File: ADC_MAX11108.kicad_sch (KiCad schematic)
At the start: 60 parts, among them IC22 524SDCGI8, IC24 524SDCGI8, IC26 524SDCGI8, IC28 524SDCGI8, IC30 LMS1585ACSX-ADJ_NOPB, J1 Conn_01x02_Pin, J2 Conn_01x03_Pin, J3 Conn_01x07_Pin, J4 Conn_01x07_Pin, J5 Conn_01x07_Pin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

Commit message: completed duplicating the ADCs in the schematic
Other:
- added sheet ADC10 (untitled.kicad_sch)
- added sheet ADC11 (untitled.kicad_sch)
- added sheet ADC12 (untitled.kicad_sch)
- added sheet ADC13 (untitled.kicad_sch)
- added sheet ADC14 (untitled.kicad_sch)
- added sheet ADC15 (untitled.kicad_sch)
- added sheet ADC16 (untitled.kicad_sch)
- added sheet ADC17 (untitled.kicad_sch)
- added sheet ADC18 (untitled.kicad_sch)
- added sheet ADC19 (untitled.kicad_sch)
- added sheet ADC2 (untitled.kicad_sch)
- added sheet ADC20 (untitled.kicad_sch)
- added sheet ADC21 (untitled.kicad_sch)
- added sheet ADC22 (untitled.kicad_sch)
- added sheet ADC23 (untitled.kicad_sch)
- added sheet ADC24 (untitled.kicad_sch)
- added sheet ADC3 (untitled.kicad_sch)
- added sheet ADC4 (untitled.kicad_sch)
- added sheet ADC5 (untitled.kicad_sch)
- added sheet ADC6 (untitled.kicad_sch)
- added sheet ADC7 (untitled.kicad_sch)
- added sheet ADC8 (untitled.kicad_sch)
- added sheet ADC9 (untitled.kicad_sch)

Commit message: Updated schematic and PCB layout, no more precision Vrefs
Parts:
- removed C194, C52, C54, C58, C59: 10uF, Capacitor_SMD:C_0402_1005Metric_Pad0.74x0.62mm_HandSolder, symbol Device:C
- removed C53, C55, C56, C57, C60, C61, C69, C71, C73: 0.1uF, Capacitor_SMD:C_0402_1005Metric_Pad0.74x0.62mm_HandSolder, symbol Device:C
- removed J2: Conn_01x03_Pin, Connector_PinHeader_2.54mm:PinHeader_1x03_P2.54mm_Vertical, symbol Connector:Conn_01x03_Pin
- removed U1, U2, U3, U4, U5: ADR4533, Package_SO:SOIC-8_3.9x4.9mm_P1.27mm, symbol Reference_Voltage:ADR4533
- added J2, J8: Conn_01x02_Pin, Connector_PinHeader_2.54mm:PinHeader_1x02_P2.54mm_Vertical, symbol Connector:Conn_01x02_Pin
- C195, C68, C70, C72: value 10uF -> 0.01uF
- C196, C197, C66, C67: value C -> 10uF
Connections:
- net 3.4V is gone; now on net 3.3_ADJ: J1.1 (Pin_1)
- net Battery_3.3V is gone; now on net Vref_LDO: Q1.2 (OUTPUT)
- net Basys_3.3V: now also J2.1 (Pin_1), J2.2 (Pin_2)
- net GND: now also C196.2, C197.2, C66.2, C67.1
- net Switch_out: now also C197.1, C67.2
- net at IC30.2 (OUTPUT), IC30.4 (VOUT_1), IC30.5 (VOUT_2)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: now also C196.1
- net Vref_LDO: now reaches C66.1
- net Vref_LDO: now also J8.2 (Pin_2)
- net +3.3V renamed 3.3_ADJ
- new net 3.3VRef: J8.1 (Pin_1)
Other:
- note added: "A 33 OHM series terminating resistor may be used on each clock output if the trace is longer than 1 inch."
- note removed: "A minimum number of external components are required for proper operation. A decoupling capacitor of 0.01µF should be connected between VDD on pin 5 and GND on pin 8, as close to the device as possible. A 33 series terminating resistor may be used on each clock output if the trace is longer than 1 inch."
- moved on the sheet: Barrel_Jack1, C196, C197, C66, C67, IC30, J1, R21, S1, VR1

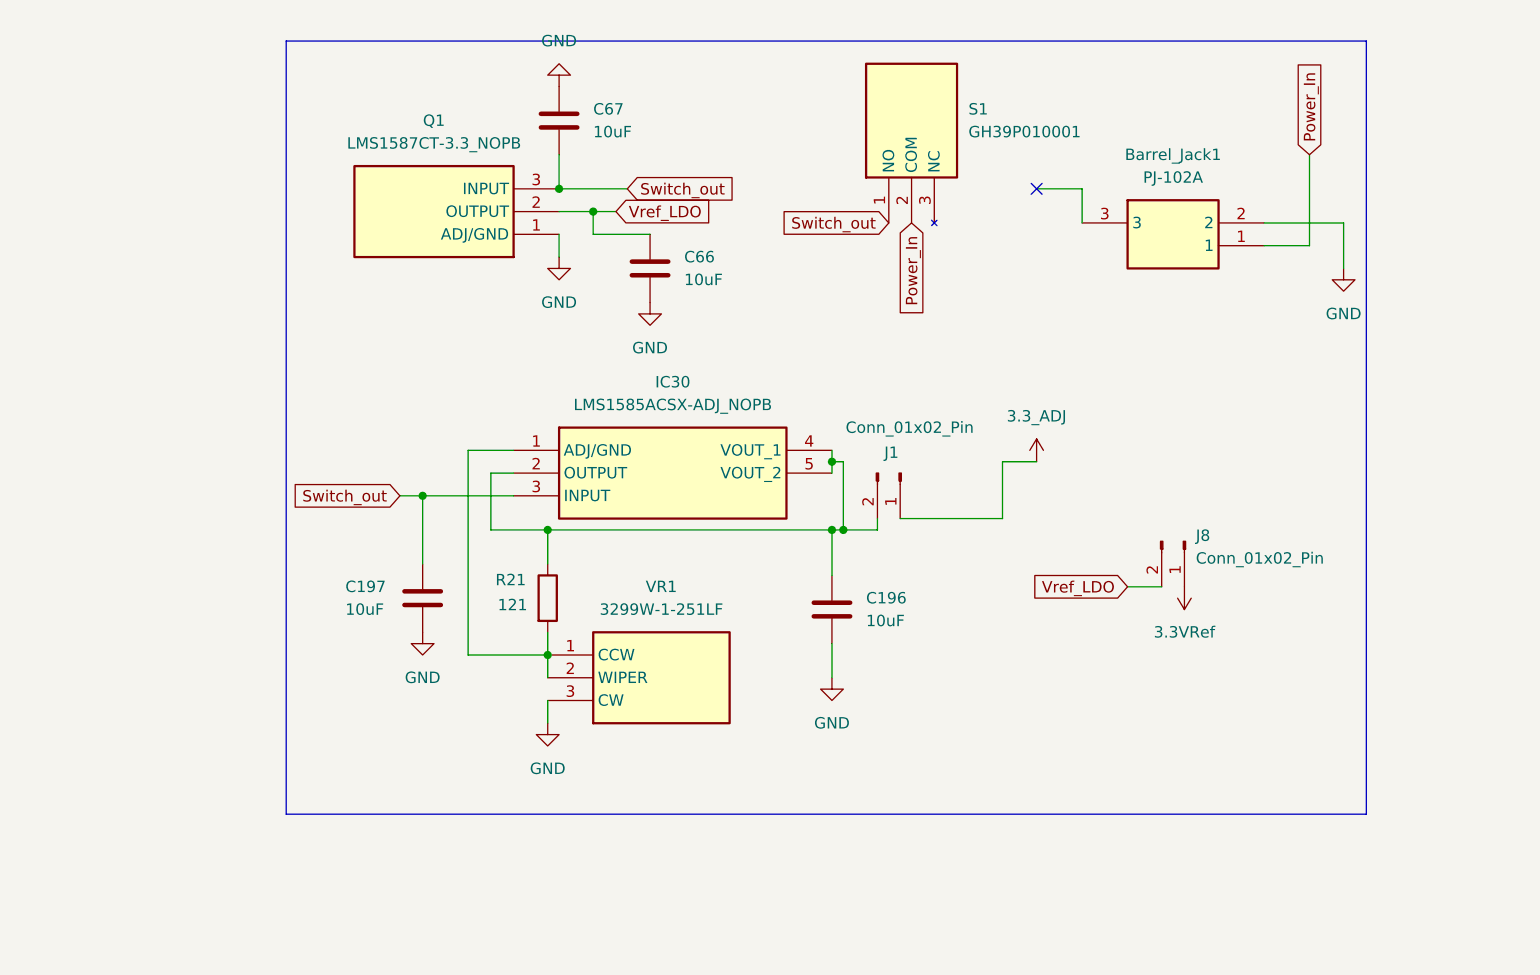
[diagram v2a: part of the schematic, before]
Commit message: Finished Power section routing, added LED indicators
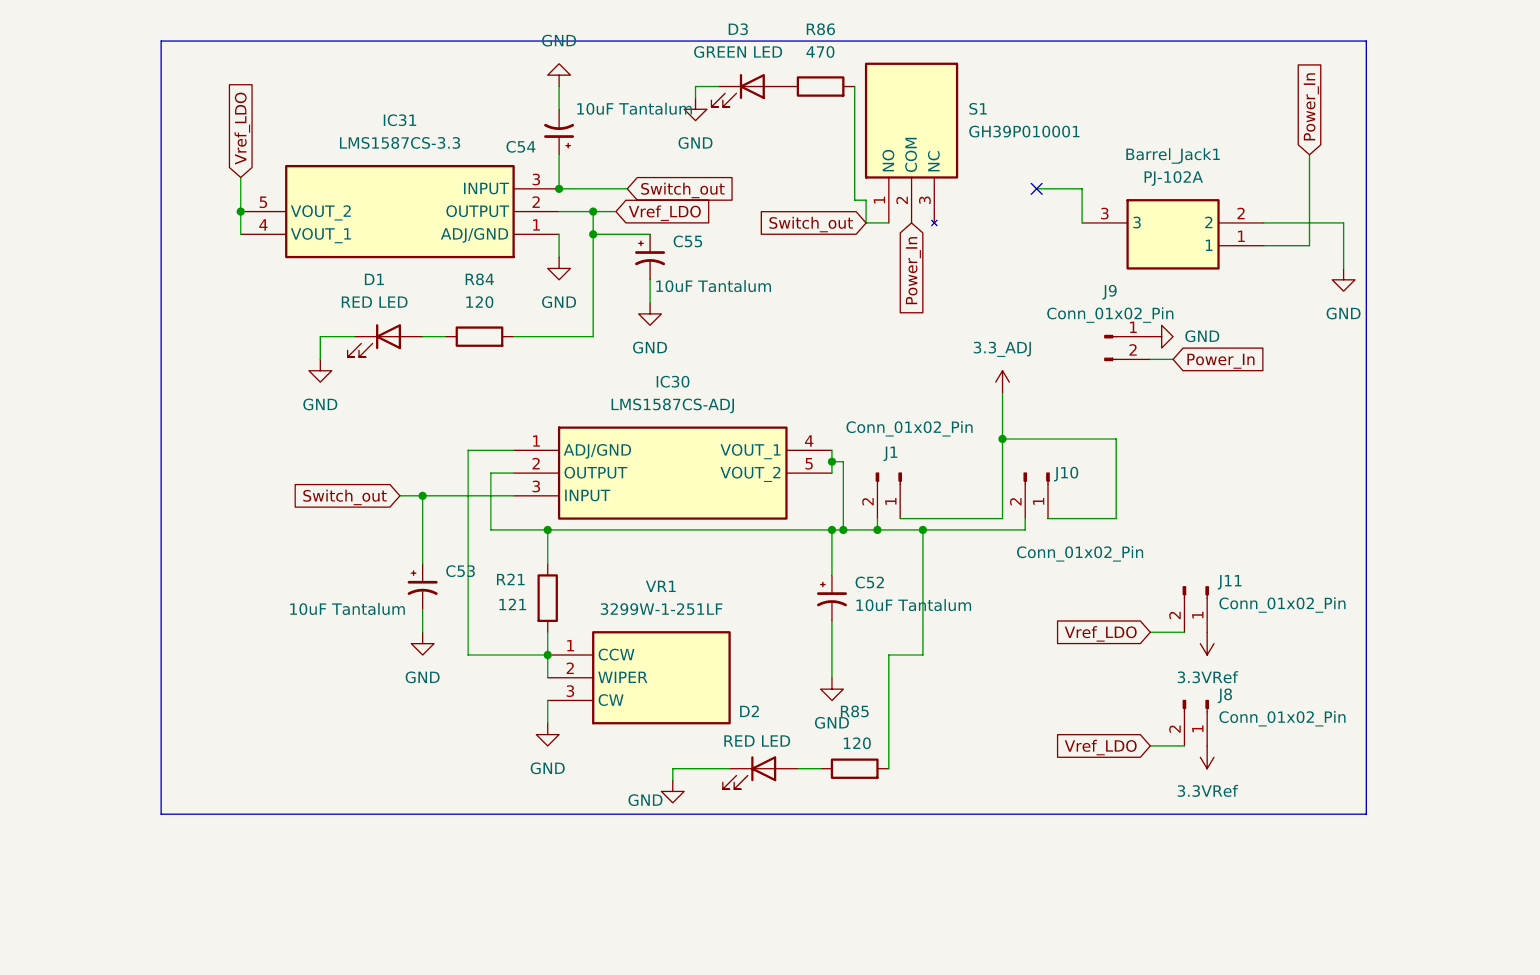
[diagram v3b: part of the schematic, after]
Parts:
- removed C196, C66, C67: 10uF, Capacitor_SMD:C_0402_1005Metric_Pad0.74x0.62mm_HandSolder, symbol Device:C
- removed C197: 10uF, Connector_PinHeader_2.54mm:PinHeader_1x02_P2.54mm_Vertical, symbol Device:C
- removed Q1: LMS1587CT-3.3_NOPB, My_footprints:LM1085ISX33NOPB, symbol Samacsys_parts:LMS1587CT-3.3_NOPB
- added C52, C53, C54, C55: 10uF Tantalum, Capacitor_Tantalum_SMD:CP_EIA-6032-28_Kemet-C_HandSolder, symbol Device:C_Polarized_Small_US
- added D1, D2: RED LED, LED_SMD:LED_0603_1608Metric_Pad1.05x0.95mm_HandSolder, symbol Device:LED
- added D3: GREEN LED, LED_SMD:LED_0603_1608Metric_Pad1.05x0.95mm_HandSolder, symbol Device:LED
- added IC31: LMS1587CS-3.3, SamacSys_Parts:LMS1587CSXADJNOPB, symbol Samacsys_parts:LMS1585ACSX-ADJ_NOPB
- added J10, J11: Conn_01x02_Pin, Connector_PinHeader_2.54mm:PinHeader_1x02_P2.54mm_Vertical, symbol Connector:Conn_01x02_Pin
- added J9: Conn_01x02_Pin, Connector_JST:JST_XA_B02B-XASK-1-A_1x02_P2.50mm_Vertical, symbol Connector:Conn_01x02_Pin
- added R84, R85: 120, Resistor_SMD:R_0603_1608Metric_Pad0.98x0.95mm_HandSolder, symbol Device:R
- added R86: 470, Resistor_SMD:R_0603_1608Metric_Pad0.98x0.95mm_HandSolder, symbol Device:R
- IC30: value LMS1585ACSX-ADJ_NOPB -> LMS1587CS-ADJ; footprint My_footprints:LM1085ISX33NOPB -> SamacSys_Parts:LMS1587CSXADJNOPB
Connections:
- net 3.3VRef: now also J11.1 (Pin_1)
- net 3.3_ADJ: now also J10.1 (Pin_1)
- net GND: now also C52.2, C53.2, C54.2, C55.2, D1.1 (K), D2.1 (K), D3.1 (K), IC31.1 (ADJ/GND), J9.1 (Pin_1)
- net Power_In: now also J9.2 (Pin_2)
- net Switch_out: now also C53.1, C54.1, IC31.3 (INPUT), R86.2
- net Vref_LDO: now also C55.1, IC31.2 (OUTPUT), IC31.4 (VOUT_1), IC31.5 (VOUT_2), J11.2 (Pin_2), R84.2
- net at IC30.2 (OUTPUT), IC30.4 (VOUT_1), IC30.5 (VOUT_2)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: now also C52.1, J10.2 (Pin_2), R85.2
- new net: D3.2 (A), R86.1
- new net: D1.2 (A), R84.1
- new net: D2.2 (A), R85.1
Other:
- moved on the sheet: J8

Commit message: Routed most of the Douts, and all of the CS & SCLK
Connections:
- net CLK_4: now also IC26.3 (Q1); no longer IC26.7 (Q3)
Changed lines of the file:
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@@
 	)
 	(no_connect
-		(at 670.56 285.75)
+		(at 698.5 283.21)
 	)
 	(no_connect
@@
 	(wire
 		(pts
+			(xy 657.86 285.75) (xy 670.56 285.75)
+		)
+		(stroke
+			(width 0)
+			(type default)
+		)
+	)
+	(wire
+		(pts
 			(xy 321.31 350.52) (xy 326.39 350.52)
 		)
@@
 	(wire
 		(pts
-			(xy 698.5 283.21) (xy 707.39 283.21)
-		)
-		(stroke
-			(width 0)
-			(type default)
-		)
-	)
-	(wire
-		(pts
 			(xy 678.18 142.24) (xy 671.83 142.24)
 		)
@@
 		)
 	)
+	(global_label "CLK_4"
+		(shape input)
+		(at 657.86 285.75 180)
+		(fields_autoplaced yes)
+		(effects
+			(font
+				(size 1.27 1.27)
+			)
+			(justify right)
+		)
+		(property "Intersheetrefs" "${INTERSHEET_REFS}"
+			(at 649.1296 285.75 0)
+			(effects
+				(font
+					(size 1.27 1.27)
+				)
+				(justify right)
+				(hide yes)
+			)
+		)
+	)
 	(global_label "B1C2_8"
 		(shape input)
@@
 			(effects
 				(font
-					(size 1.27 1.27)
-				)
-				(justify left)
-				(hide yes)
-			)
-		)
-	)
-	(global_label "CLK_4"
-		(shape input)
-		(at 707.39 283.21 0)
-		(fields_autoplaced yes)
-		(effects
-			(font
-				(size 1.27 1.27)
-			)
-			(justify left)
-		)
-		(property "Intersheetrefs" "${INTERSHEET_REFS}"
-			(at 716.1204 283.21 0)
-			(effects
-				(font
